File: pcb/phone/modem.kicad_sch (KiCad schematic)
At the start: 10 parts, among them U2 PCIE-52P40H_C444926, U3 TXB0108PWR

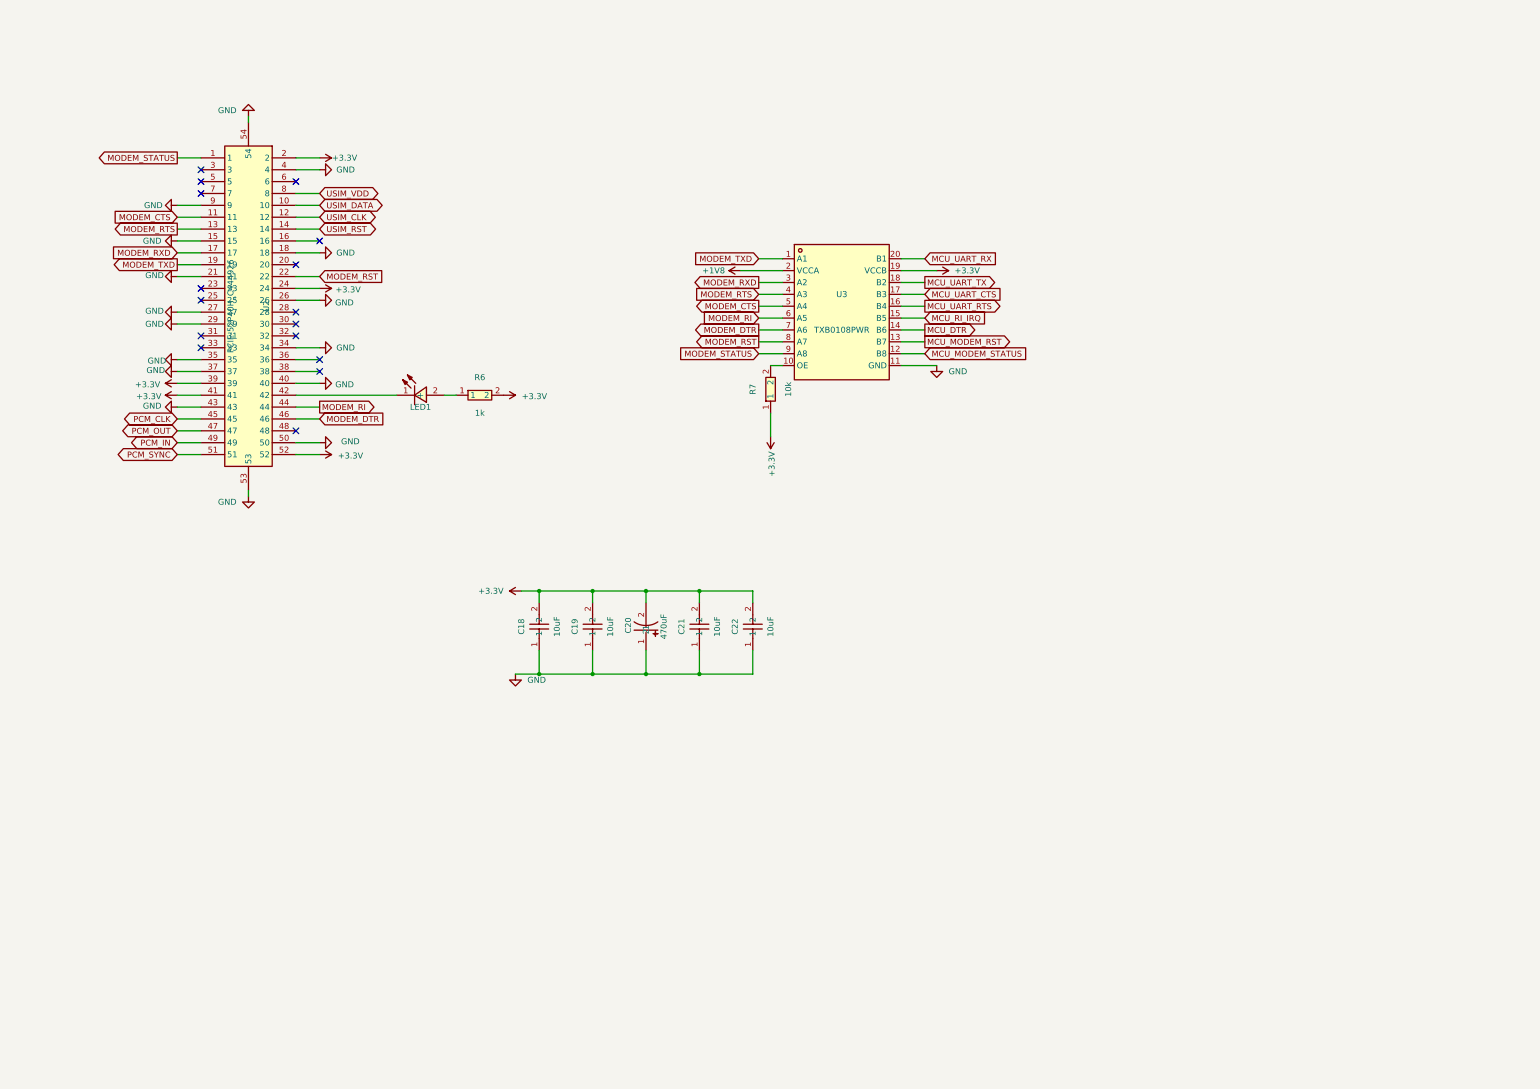
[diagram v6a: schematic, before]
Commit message: Pivot form factor to candybar/single-board + doc-audit fixes
Flip/clamshell (two PCBs + hinge flex) → candybar (single PCB). Drops
outer display, hinge flex connectors (J8/J9), daughterboard. Display
mounts directly via J7 ZIF. Backlight FET architecture conflict resolved
(FET on single board). See project-log.md 2026-08-16.

Doc-audit caught 4 stale references the pivot session missed:
- datasheets/README.md: ST7789V.pdf desc, ER-TFT1.14-2 row, outer display
  raw panel line — all marked DROPPED
- ic-by-ic-review.md: ST7789 outer display row + Display_Daughter sheet
  reference — marked DROPPED

KiCad: modem/phone/power sheets + PCB updated for single-board design.

Generated with [Devin](https://devin.ai)

Co-Authored-By: Devin <158243242+devin-ai-integration[bot]@users.noreply.github.com>
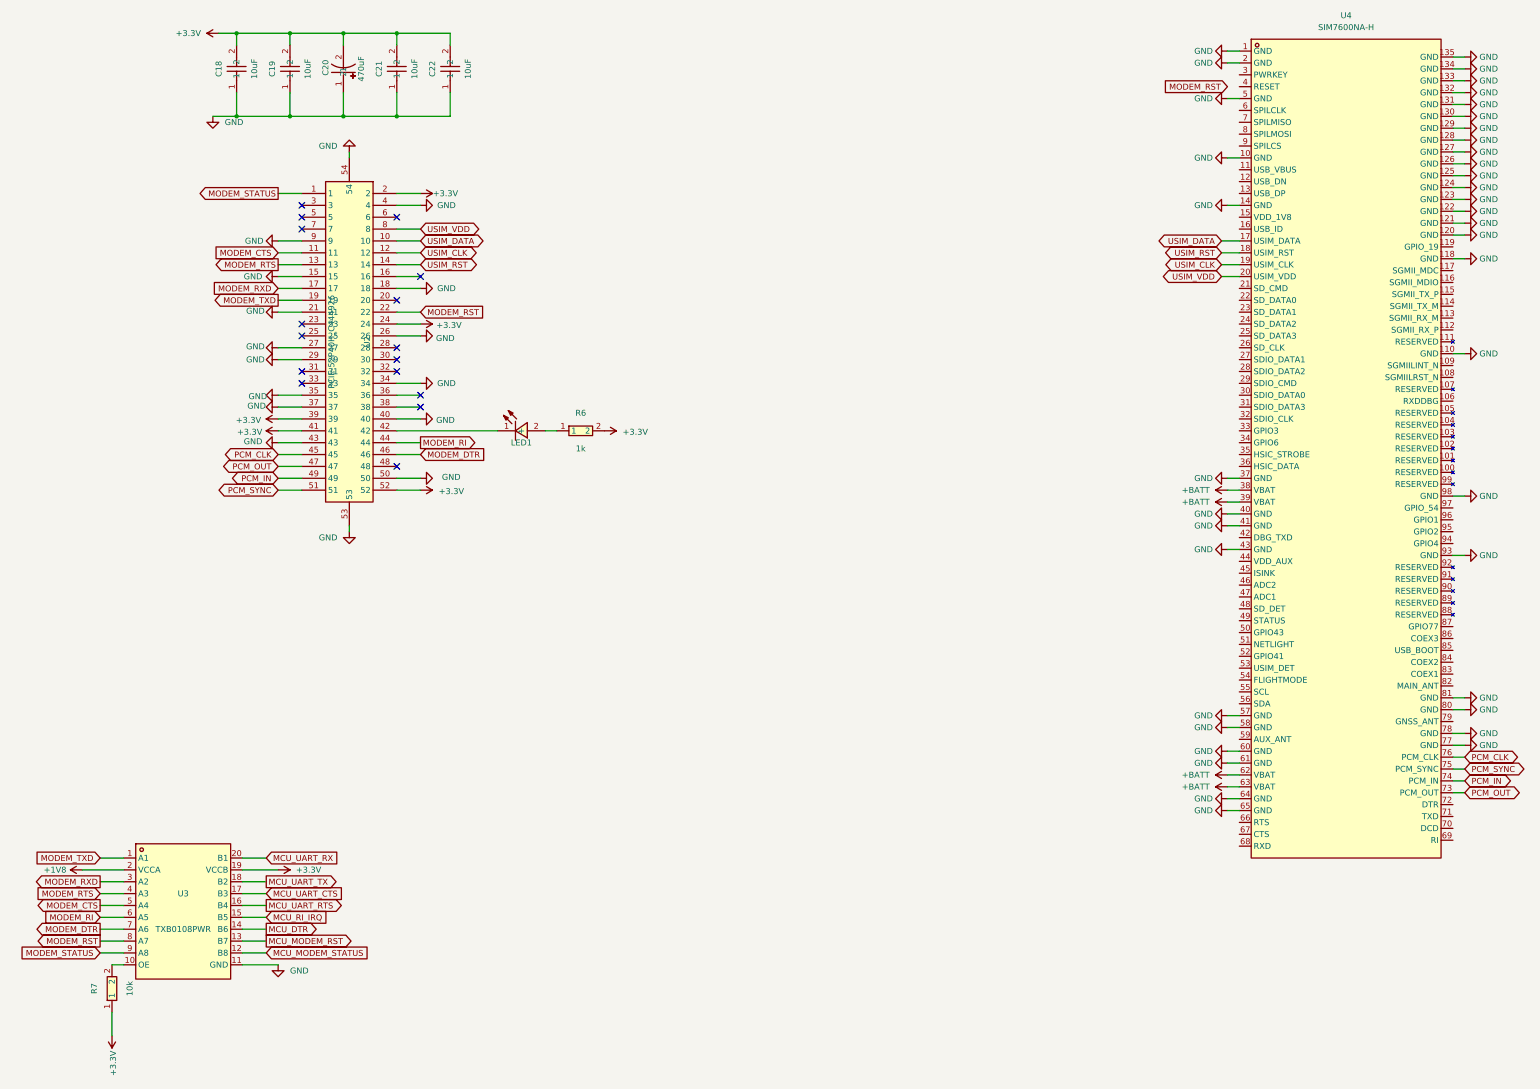
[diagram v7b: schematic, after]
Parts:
- added U4: SIM7600NA-H, easyeda2kicad:COMM-SMD_L13.0-W13.0-P1.0_SIM7600NA-H, symbol ics:SIM7600NA-H
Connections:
- net GND: now also U4.1 (GND), U4.10 (GND), U4.110 (GND), U4.118 (GND), U4.120 (GND), U4.121 (GND), U4.122 (GND), U4.123 (GND), U4.124 (GND), U4.125 (GND), U4.126 (GND), U4.127 (GND), U4.128 (GND), U4.129 (GND), U4.130 (GND), U4.131 (GND), U4.132 (GND), U4.133 (GND), U4.134 (GND), U4.135 (GND), U4.14 (GND), U4.2 (GND), U4.37 (GND), U4.40 (GND), U4.41 (GND), U4.43 (GND), U4.5 (GND), U4.57 (GND), U4.58 (GND), U4.60 (GND), U4.61 (GND), U4.64 (GND), U4.65 (GND), U4.77 (GND), U4.78 (GND), U4.80 (GND), U4.81 (GND), U4.93 (GND), U4.98 (GND)
- net PCM_CLK: now also U4.76 (PCM_CLK)
- net PCM_IN: now also U4.74 (PCM_IN)
- net PCM_OUT: now also U4.73 (PCM_OUT)
- net PCM_SYNC: now also U4.75 (PCM_SYNC)
- net USIM_CLK: now also U4.19 (USIM_CLK)
- net USIM_DATA: now also U4.17 (USIM_DATA)
- net USIM_RST: now also U4.18 (USIM_RST)
- net USIM_VDD: now also U4.20 (USIM_VDD)
- new net +BATT: U4.38 (VBAT), U4.39 (VBAT), U4.62 (VBAT), U4.63 (VBAT)
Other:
- moved on the sheet: C18, C19, C20, C21, C22, LED1, R6, R7, U2, U3
